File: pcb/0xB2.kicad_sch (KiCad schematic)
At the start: 39 parts, among them J1 USB_C_Receptacle_USB2.0, J2 Conn_01x12, J3 Conn_01x05, J4 Conn_01x12, SW1 SW_Push, SW2 SW_Push, U1 RP2040, U2 W25Q32JVZP, U3 XC6210B332MR-G, Y1 Crystal_GND24

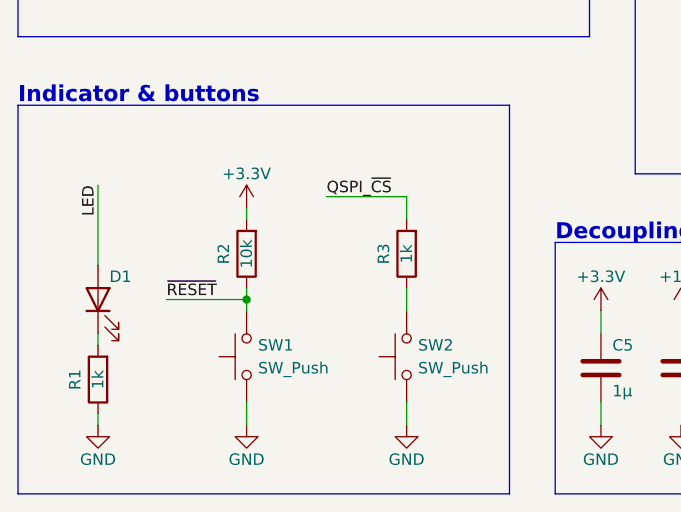
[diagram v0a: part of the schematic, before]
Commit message: Add pins for BOOT from the back
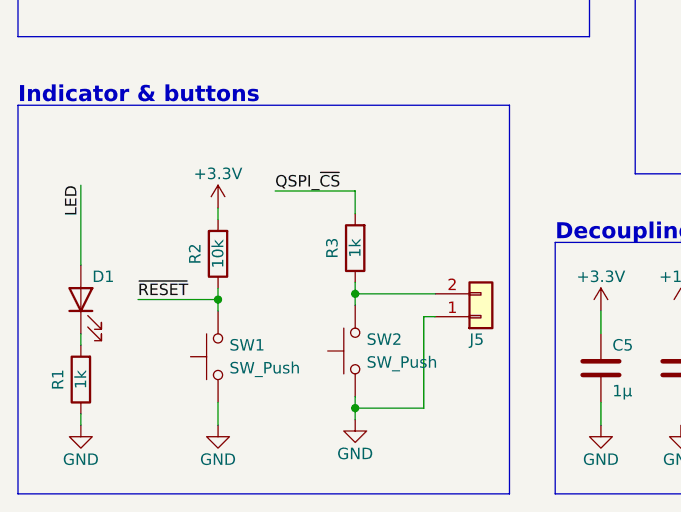
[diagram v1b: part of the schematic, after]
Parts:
- added J5: Conn_01x02, Connector_PinHeader_1.27mm:PinHeader_1x02_P1.27mm_Vertical, symbol Connector_Generic:Conn_01x02
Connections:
- net GND: now also J5.1 (Pin_1)
- net at R3.1, SW2.2: now also J5.2 (Pin_2)
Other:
- moved on the sheet: D1, R1, R2, R3, SW1, SW2

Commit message: README and doc update
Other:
- title: 0xB2 - blinky2040 -> 0xB2 - Splinky
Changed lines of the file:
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@@
   (paper "A4")
   (title_block
-    (title "0xB2 - blinky2040")
-    (rev "v0")
+    (title "0xB2 - Splinky")
+    (rev "2")
     (company "plut0nium")
   )

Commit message: Get v2 ready for manufacturing
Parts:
- J2, J3, J4, J5: now left out of the parts list
- U2: value W25Q32JVZP -> GD25Q80CEIGR
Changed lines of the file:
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@@
   )
   (symbol (lib_id "Connector_Generic:Conn_01x02") (at 69.215 174.625 0) (mirror x) (unit 1)
-    (in_bom yes) (on_board yes)
+    (in_bom no) (on_board yes)
     (property "Reference" "J5" (id 0) (at 67.945 177.165 0)
       (effects (font (size 1.27 1.27)) (justify left))
@@
   )
   (symbol (lib_id "Connector_Generic:Conn_01x05") (at 246.38 86.36 90) (mirror x) (unit 1)
-    (in_bom yes) (on_board yes)
+    (in_bom no) (on_board yes)
     (property "Reference" "J3" (id 0) (at 238.76 86.36 90))
     (property "Value" "Conn_01x05" (id 1) (at 246.38 88.9 90))
@@
       (effects (font (size 1.27 1.27)) (justify left))
     )
-    (property "Value" "W25Q32JVZP" (id 1) (at 245.8594 121.92 0)
+    (property "Value" "GD25Q80CEIGR" (id 1) (at 245.8594 121.92 0)
       (effects (font (size 1.27 1.27)) (justify left))
     )
@@
       (effects (font (size 1.27 1.27)) hide)
     )
-    (property "Datasheet" "http://www.winbond.com/resource-files/w25q32jv%20revg%2003272018%20plus.pdf" (id 3) (at 243.84 132.08 0)
+    (property "Datasheet" "" (id 3) (at 243.84 132.08 0)
       (effects (font (size 1.27 1.27)) hide)
     )
@@
   )
   (symbol (lib_id "Connector_Generic:Conn_01x12") (at 223.52 52.07 0) (mirror y) (unit 1)
-    (in_bom yes) (on_board yes)
+    (in_bom no) (on_board yes)
     (property "Reference" "J2" (id 0) (at 223.52 36.83 0))
     (property "Value" "Conn_01x12" (id 1) (at 220.98 52.07 90))
@@
   )
   (symbol (lib_id "Connector_Generic:Conn_01x12") (at 269.24 54.61 0) (mirror x) (unit 1)
-    (in_bom yes) (on_board yes)
+    (in_bom no) (on_board yes)
     (property "Reference" "J4" (id 0) (at 269.24 36.83 0))
     (property "Value" "Conn_01x12" (id 1) (at 271.78 52.07 90))
@@
     )
     (path "/3b628cb4-77fa-40d4-8aa3-0ae0b973ec32"
-      (reference "U2") (unit 1) (value "W25Q32JVZP") (footprint "0xLib_Package_DFN_QFN:USON-8-1EP_3x2mm_P0.5mm_EP0.25x1.65mm")
+      (reference "U2") (unit 1) (value "GD25Q80CEIGR") (footprint "0xLib_Package_DFN_QFN:USON-8-1EP_3x2mm_P0.5mm_EP0.25x1.65mm")
     )
     (path "/33208a57-5054-4bad-b85f-35da7b25e7bb"

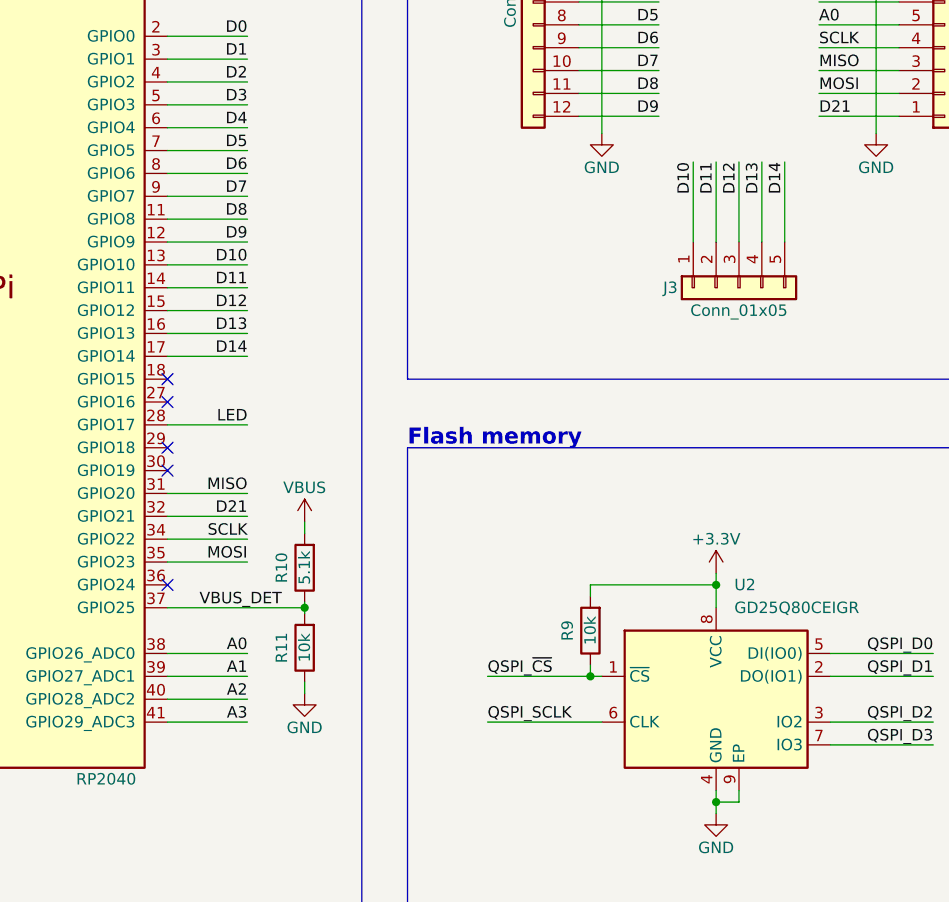
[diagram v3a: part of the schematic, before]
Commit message: Update pinout
Use of the agreed pinout (see discussions on bkb discord)
for bottom row and VBUS detect.
Maintain compatibility with Sparkfun RP2040.
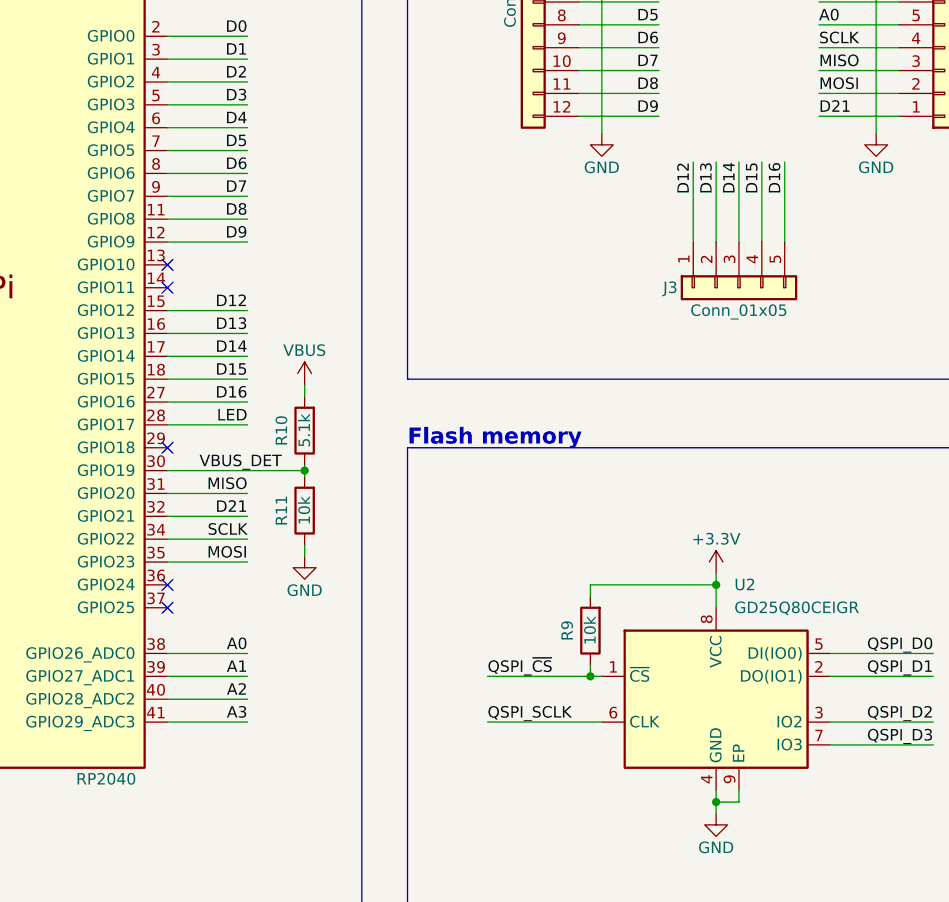
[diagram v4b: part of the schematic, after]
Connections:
- net D12: now also J3.1 (Pin_1); no longer J3.3 (Pin_3)
- net D13: now also J3.2 (Pin_2); no longer J3.4 (Pin_4)
- net D14: now also J3.3 (Pin_3); no longer J3.5 (Pin_5)
- net VBUS_DET: now also U1.30 (GPIO19); no longer U1.37 (GPIO25)
- net D15: now reaches U1.18 (GPIO15)
- net D15: now also J3.4 (Pin_4)
- net D16: now reaches U1.27 (GPIO16)
- net D16: now also J3.5 (Pin_5)
- net D10: no longer names the net of U1.13 (GPIO10)
- net D10: no longer J3.1 (Pin_1)
- net D11: no longer names the net of U1.14 (GPIO11)
- net D11: no longer J3.2 (Pin_2)
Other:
- moved on the sheet: R10, R11

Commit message: Switch USB-C connector
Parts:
- J1: footprint 0xLib_USB_Type-C:USB_C_Receptacle_HRO_TYPE-C-31-M-14 -> 0xLib_USB_Type-C:USB_C_Receptacle_HRO_TYPE-C-31-M-13B; LCSC C223907 -> C2848619
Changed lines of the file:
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@@
     (property "Reference" "J1" (id 0) (at 35.56 29.21 0))
     (property "Value" "USB_C_Receptacle_USB2.0" (id 1) (at 35.56 31.75 0))
-    (property "Footprint" "0xLib_USB_Type-C:USB_C_Receptacle_HRO_TYPE-C-31-M-14" (id 2) (at 39.37 52.07 0)
+    (property "Footprint" "0xLib_USB_Type-C:USB_C_Receptacle_HRO_TYPE-C-31-M-13B" (id 2) (at 39.37 52.07 0)
       (effects (font (size 1.27 1.27)) hide)
     )
@@
       (effects (font (size 1.27 1.27)) hide)
     )
-    (property "LCSC" "C223907" (id 4) (at 35.56 52.07 0)
+    (property "LCSC" "C2848619" (id 4) (at 35.56 52.07 0)
       (effects (font (size 1.27 1.27)) hide)
     )
@@
     )
     (path "/6125bb34-31fe-49ed-b2ab-61dab24d450a"
-      (reference "J1") (unit 1) (value "USB_C_Receptacle_USB2.0") (footprint "0xLib_USB_Type-C:USB_C_Receptacle_HRO_TYPE-C-31-M-14")
+      (reference "J1") (unit 1) (value "USB_C_Receptacle_USB2.0") (footprint "0xLib_USB_Type-C:USB_C_Receptacle_HRO_TYPE-C-31-M-13B")
     )
     (path "/44683f1e-d2b9-4133-9a9d-84586c32a6a2"
